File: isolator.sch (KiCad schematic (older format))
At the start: 21 parts, among them U101 NE5532

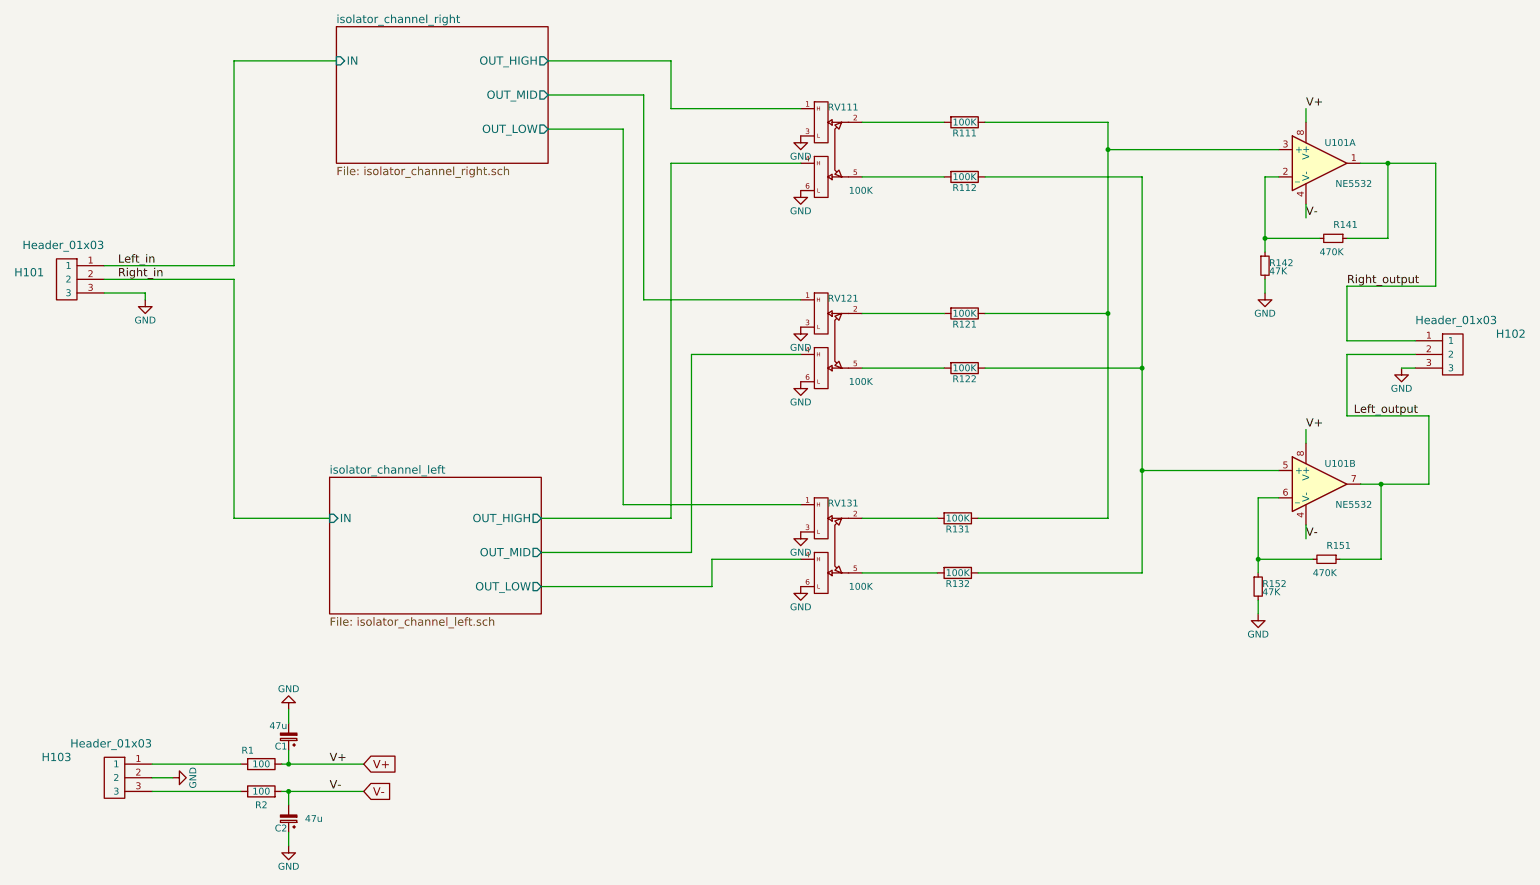
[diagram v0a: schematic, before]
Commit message: Adding active components references
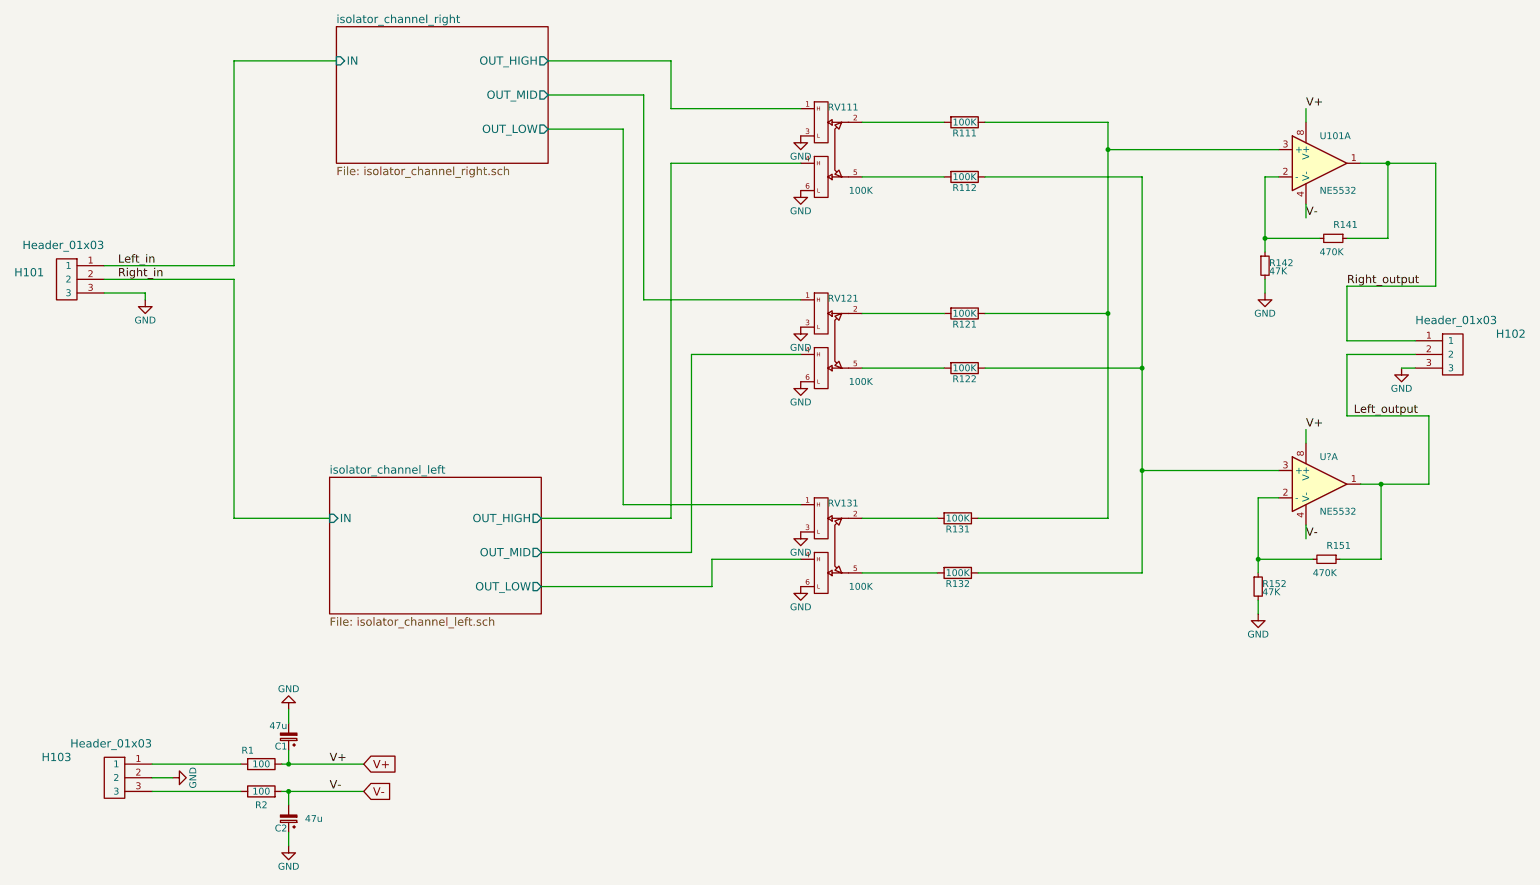
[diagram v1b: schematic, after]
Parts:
- removed U101: NE5532, Housings_DIP:DIP-8_W7.62mm_LongPads, symbol NE5532-RESCUE-isolator
- added U101, U?: NE5532, Housings_DIP:DIP-8_W7.62mm_LongPads, symbol NE5532
- R111, R112, R121, R122, R131, R132: Description (none) -> Résistances à couche métallique - Trou traversant 1/3watts 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; Distributor (none) -> Mouser; Distributor Part # (none) -> 71-CCF50-100K; Manufacturer (none) -> Vishay / Dale; Mfg_Part_# (none) -> CCF50100KFKR36; Package (none) -> 2-THT
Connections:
- net Left_output: now also U?.1
- net Right_output: now also U101.1
- net V+: now also U101.8 (V+), U?.8 (V+)
- net V-: now also U101.4 (V-), U?.4 (V-)
- net at R111.1, R121.1, R131.1: now also U101.3 (+)
- net at R112.1, R122.1, R132.1: now also U?.3 (+)
- net at R141.2, R142.1: now also U101.2 (-)
- net at R151.2, R152.1: now also U?.2 (-)

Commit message: Updating components footprints
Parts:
- gave numbers to parts that had none: 1
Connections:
- net Left_output: now also U101.7; no longer U101.1
- net at R151.2, R152.1: now also U101.6 (-); no longer U101.2 (-)
- net at R112.1, R122.1, R132.1: now also U101.5 (+); no longer U101.3 (+)
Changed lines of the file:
@@
 $EndComp
 $Comp
-L NE5532 U?
-U 1 1 5A0D725C
+L NE5532 U101
+U 2 1 5A0D725C
 P 10100 4700
-F 0 "U?" H 10100 4900 50  0000 L CNN
+F 0 "U101" H 10100 4900 50  0000 L CNN
 F 1 "NE5532" H 10100 4500 50  0000 L CNN
 F 2 "Housings_DIP:DIP-8_W7.62mm_LongPads" H 10100 4700 50  0001 C CNN
@@
 F 8 "Amplificateurs opérationnels - Amplis-Op Dual Low Noise" H 10100 4700 60  0001 C CNN "Description"
 F 9 "Texas Instruments" H 10100 4700 60  0001 C CNN "Manufacturer"
-	1    10100 4700
+	2    10100 4700
 	1    0    0    -1
 $EndComp

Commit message: Updating components references and properties
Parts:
- R111, R112, R121, R122, R131, R132, R141, R142, R151, R152: footprint Resistors_ThroughHole:Resistor_Horizontal_RM7mm -> Resistors_THT:R_Axial_DIN0204_L3.6mm_D1.6mm_P5.08mm_Horizontal
- RV111, RV121, RV131: footprint ALPS_pot:Potentiometer_ALPS_RK27112A0A16 -> potentiometers:Potentiometer_ALPS_RK27; Description (none) -> Potentiomètres Flat 20mm 100k; Distributor (none) -> Mouser; Distributor Part # (none) -> 688-RK27112A0A16; Manufacturer (none) -> ALPS; Mfg_Part_# (none) -> RK27112A0A16; Package (none) -> RK27
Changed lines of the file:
@@
 F 0 "RV111" H 6610 2560 50  0000 C CNN
 F 1 "100K" H 6740 1950 50  0000 C CNN
-F 2 "ALPS_pot:Potentiometer_ALPS_RK27112A0A16" H 6450 2250 50  0001 C CNN
-F 3 "" H 6450 2250 50  0000 C CNN
-F 4 "RK27112A0A16" H 6450 2250 60  0001 C CNN "Mfg_Part_No"
+F 2 "potentiometers:Potentiometer_ALPS_RK27" H 6450 2250 50  0001 C CNN
+F 3 "http://www.alps.com/products/WebObjects/catalog.woa/E/HTML/Potentiometer/RotaryPotentiometers/RK271/RK27112A0A16.html" H 6450 2250 50  0001 C CNN
+F 4 "RK27112A0A16" H 6450 2250 60  0001 C CNN "Mfg_Part_#"
+F 5 "Mouser" H 6450 2250 60  0001 C CNN "Distributor"
+F 6 "688-RK27112A0A16" H 6450 2250 60  0001 C CNN "Distributor Part #"
+F 7 "RK27" H 6450 2250 60  0001 C CNN "Package"
+F 8 "Potentiomètres Flat 20mm 100k" H 6450 2250 60  0001 C CNN "Description"
+F 9 "ALPS" H 6450 2250 60  0001 C CNN "Manufacturer"
+F 10 "RK27112A0A16" H 6450 2250 60  0001 C CNN "Mfg_Part_No"
 	1    6450 2250
-	1    0    0    -1
-$EndComp
-$Comp
-L DUAL_POT RV121
-U 1 1 56D771AD
-P 6450 3650
-F 0 "RV121" H 6610 3960 50  0000 C CNN
-F 1 "100K" H 6740 3350 50  0000 C CNN
-F 2 "ALPS_pot:Potentiometer_ALPS_RK27112A0A16" H 6450 3650 50  0001 C CNN
-F 3 "" H 6450 3650 50  0000 C CNN
-F 4 "RK27112A0A16" H 6450 3650 60  0001 C CNN "Mfg_Part_No"
-	1    6450 3650
-	1    0    0    -1
-$EndComp
-$Comp
-L DUAL_POT RV131
-U 1 1 56D7724C
-P 6450 5150
-F 0 "RV131" H 6610 5460 50  0000 C CNN
-F 1 "100K" H 6740 4850 50  0000 C CNN
-F 2 "ALPS_pot:Potentiometer_ALPS_RK27112A0A16" H 6450 5150 50  0001 C CNN
-F 3 "" H 6450 5150 50  0000 C CNN
-F 4 "RK27112A0A16" H 6450 5150 60  0001 C CNN "Mfg_Part_No"
-	1    6450 5150
 	1    0    0    -1
 $EndComp
@@
 F 0 "R121" V 7580 3450 50  0000 C CNN
 F 1 "100K" V 7500 3450 50  0000 C CNN
-F 2 "Resistors_ThroughHole:Resistor_Horizontal_RM7mm" V 7430 3450 50  0001 C CNN
+F 2 "Resistors_THT:R_Axial_DIN0204_L3.6mm_D1.6mm_P5.08mm_Horizontal" V 7430 3450 50  0001 C CNN
 F 3 "http://www.mouser.com/ds/2/427/ccf50-239758.pdf" H 7500 3450 50  0001 C CNN
 F 4 "CCF50100KFKR36" H 7500 3450 60  0001 C CNN "Mfg_Part_#"
@@
 	7650 2450 8800 2450
 Wire Wire Line
-	8800 2450 8800 3850
-Wire Wire Line
-	8800 3850 8800 4600
-Wire Wire Line
-	8800 4600 8800 5350
+	8800 2450 8800 5350
 Wire Wire Line
 	8800 3850 7650 3850
@@
 	8550 4950 7600 4950
 Wire Wire Line
-	8550 2050 8550 2250
-Wire Wire Line
-	8550 2250 8550 3450
-Wire Wire Line
-	8550 3450 8550 4950
+	8550 2050 8550 4950
 Wire Wire Line
 	8550 3450 7650 3450
@@
 F 0 "R142" H 9730 3120 50  0000 L CNN
 F 1 "47K" H 9730 3060 50  0000 L CNN
-F 2 "Resistors_ThroughHole:Resistor_Horizontal_RM7mm" H 9700 3100 50  0001 C CNN
+F 2 "Resistors_THT:R_Axial_DIN0204_L3.6mm_D1.6mm_P5.08mm_Horizontal" H 9700 3100 50  0001 C CNN
 F 3 "" H 9700 3100 50  0000 C CNN
 F 4 "CCF0747K0JKE36" H 9700 3100 60  0001 C CNN "Mfg_Part_No"
@@
 F 0 "R141" V 10100 2900 50  0000 L CNN
 F 1 "470K" V 10300 2800 50  0000 L CNN
-F 2 "Resistors_ThroughHole:Resistor_Horizontal_RM7mm" H 10200 2900 50  0001 C CNN
+F 2 "Resistors_THT:R_Axial_DIN0204_L3.6mm_D1.6mm_P5.08mm_Horizontal" H 10200 2900 50  0001 C CNN
 F 3 "" H 10200 2900 50  0000 C CNN
 F 4 "CCF07470KGKE36" H 10200 2900 60  0001 C CNN "Mfg_Part_No"
@@
 	9800 2450 9700 2450
 Wire Wire Line
-	9700 2450 9700 2900
-Wire Wire Line
-	9700 2900 9700 3000
+	9700 2450 9700 3000
 Wire Wire Line
 	10100 2900 9700 2900
 Connection ~ 9700 2900
 Wire Wire Line
-	10400 2350 10600 2350
-Wire Wire Line
-	10600 2350 10950 2350
+	10400 2350 10950 2350
 Wire Wire Line
 	10600 2350 10600 2900
@@
 F 0 "R152" H 9680 5470 50  0000 L CNN
 F 1 "47K" H 9680 5410 50  0000 L CNN
-F 2 "Resistors_ThroughHole:Resistor_Horizontal_RM7mm" H 9650 5450 50  0001 C CNN
+F 2 "Resistors_THT:R_Axial_DIN0204_L3.6mm_D1.6mm_P5.08mm_Horizontal" H 9650 5450 50  0001 C CNN
 F 3 "" H 9650 5450 50  0000 C CNN
 F 4 "CCF0747K0JKE36" H 9650 5450 60  0001 C CNN "Mfg_Part_No"
@@
 F 0 "R151" V 10050 5250 50  0000 L CNN
 F 1 "470K" V 10250 5150 50  0000 L CNN
-F 2 "Resistors_ThroughHole:Resistor_Horizontal_RM7mm" H 10150 5250 50  0001 C CNN
+F 2 "Resistors_THT:R_Axial_DIN0204_L3.6mm_D1.6mm_P5.08mm_Horizontal" H 10150 5250 50  0001 C CNN
 F 3 "" H 10150 5250 50  0000 C CNN
 F 4 "CCF07470KGKE36" H 10150 5250 60  0001 C CNN "Mfg_Part_No"
@@
 $EndComp
 Wire Wire Line
-	9650 4800 9650 5250
-Wire Wire Line
-	9650 5250 9650 5350
+	9650 4800 9650 5350
 Wire Wire Line
 	10050 5250 9650 5250
@@
 	9800 4800 9650 4800
 Wire Wire Line
-	10400 4700 10550 4700
-Wire Wire Line
-	10550 4700 10900 4700
+	10400 4700 10900 4700
 $Comp
 L Header_01x03 H102
@@
 $EndComp
 Wire Wire Line
-	2500 6750 2550 6750
-Wire Wire Line
-	2550 6750 3100 6750
+	2500 6750 3100 6750
 Wire Wire Line
 	2550 6750 2550 6650
 Connection ~ 2550 6750
 Wire Wire Line
-	2500 6950 2550 6950
-Wire Wire Line
-	2550 6950 3100 6950
+	2500 6950 3100 6950
 Wire Wire Line
 	2550 7050 2550 6950
@@
 F 0 "R122" V 7580 3850 50  0000 C CNN
 F 1 "100K" V 7500 3850 50  0000 C CNN
-F 2 "Resistors_ThroughHole:Resistor_Horizontal_RM7mm" V 7430 3850 50  0001 C CNN
+F 2 "Resistors_THT:R_Axial_DIN0204_L3.6mm_D1.6mm_P5.08mm_Horizontal" V 7430 3850 50  0001 C CNN
 F 3 "http://www.mouser.com/ds/2/427/ccf50-239758.pdf" H 7500 3850 50  0001 C CNN
 F 4 "CCF50100KFKR36" H 7500 3850 60  0001 C CNN "Mfg_Part_#"
@@
 F 0 "R111" V 7580 2050 50  0000 C CNN
 F 1 "100K" V 7500 2050 50  0000 C CNN
-F 2 "Resistors_ThroughHole:Resistor_Horizontal_RM7mm" V 7430 2050 50  0001 C CNN
+F 2 "Resistors_THT:R_Axial_DIN0204_L3.6mm_D1.6mm_P5.08mm_Horizontal" V 7430 2050 50  0001 C CNN
 F 3 "http://www.mouser.com/ds/2/427/ccf50-239758.pdf" H 7500 2050 50  0001 C CNN
 F 4 "CCF50100KFKR36" H 7500 2050 60  0001 C CNN "Mfg_Part_#"
@@
 F 0 "R112" V 7580 2450 50  0000 C CNN
 F 1 "100K" V 7500 2450 50  0000 C CNN
-F 2 "Resistors_ThroughHole:Resistor_Horizontal_RM7mm" V 7430 2450 50  0001 C CNN
+F 2 "Resistors_THT:R_Axial_DIN0204_L3.6mm_D1.6mm_P5.08mm_Horizontal" V 7430 2450 50  0001 C CNN
 F 3 "http://www.mouser.com/ds/2/427/ccf50-239758.pdf" H 7500 2450 50  0001 C CNN
 F 4 "CCF50100KFKR36" H 7500 2450 60  0001 C CNN "Mfg_Part_#"
@@
 F 0 "R131" V 7530 4950 50  0000 C CNN
 F 1 "100K" V 7450 4950 50  0000 C CNN
-F 2 "Resistors_ThroughHole:Resistor_Horizontal_RM7mm" V 7380 4950 50  0001 C CNN
+F 2 "Resistors_THT:R_Axial_DIN0204_L3.6mm_D1.6mm_P5.08mm_Horizontal" V 7380 4950 50  0001 C CNN
 F 3 "http://www.mouser.com/ds/2/427/ccf50-239758.pdf" H 7450 4950 50  0001 C CNN
 F 4 "CCF50100KFKR36" H 7450 4950 60  0001 C CNN "Mfg_Part_#"
@@
 F 0 "R132" V 7530 5350 50  0000 C CNN
 F 1 "100K" V 7450 5350 50  0000 C CNN
-F 2 "Resistors_ThroughHole:Resistor_Horizontal_RM7mm" V 7380 5350 50  0001 C CNN
+F 2 "Resistors_THT:R_Axial_DIN0204_L3.6mm_D1.6mm_P5.08mm_Horizontal" V 7380 5350 50  0001 C CNN
 F 3 "http://www.mouser.com/ds/2/427/ccf50-239758.pdf" H 7450 5350 50  0001 C CNN
 F 4 "CCF50100KFKR36" H 7450 5350 60  0001 C CNN "Mfg_Part_#"
@@
 	0    1    1    0
 $EndComp
+$Comp
+L DUAL_POT RV121
+U 1 1 5A0D74C1
+P 6450 3650
+F 0 "RV121" H 6610 3960 50  0000 C CNN
+F 1 "100K" H 6740 3350 50  0000 C CNN
+F 2 "potentiometers:Potentiometer_ALPS_RK27" H 6450 3650 50  0001 C CNN
+F 3 "http://www.alps.com/products/WebObjects/catalog.woa/E/HTML/Potentiometer/RotaryPotentiometers/RK271/RK27112A0A16.html" H 6450 3650 50  0001 C CNN
+F 4 "RK27112A0A16" H 6450 3650 60  0001 C CNN "Mfg_Part_#"
+F 5 "Mouser" H 6450 3650 60  0001 C CNN "Distributor"
+F 6 "688-RK27112A0A16" H 6450 3650 60  0001 C CNN "Distributor Part #"
+F 7 "RK27" H 6450 3650 60  0001 C CNN "Package"
+F 8 "Potentiomètres Flat 20mm 100k" H 6450 3650 60  0001 C CNN "Description"
+F 9 "ALPS" H 6450 3650 60  0001 C CNN "Manufacturer"
+F 10 "RK27112A0A16" H 6450 3650 60  0001 C CNN "Mfg_Part_No"
+	1    6450 3650
+	1    0    0    -1
+$EndComp
+$Comp
+L DUAL_POT RV131
+U 1 1 5A0D77F6
+P 6450 5150
+F 0 "RV131" H 6610 5460 50  0000 C CNN
+F 1 "100K" H 6740 4850 50  0000 C CNN
+F 2 "potentiometers:Potentiometer_ALPS_RK27" H 6450 5150 50  0001 C CNN
+F 3 "http://www.alps.com/products/WebObjects/catalog.woa/E/HTML/Potentiometer/RotaryPotentiometers/RK271/RK27112A0A16.html" H 6450 5150 50  0001 C CNN
+F 4 "RK27112A0A16" H 6450 5150 60  0001 C CNN "Mfg_Part_#"
+F 5 "Mouser" H 6450 5150 60  0001 C CNN "Distributor"
+F 6 "688-RK27112A0A16" H 6450 5150 60  0001 C CNN "Distributor Part #"
+F 7 "RK27" H 6450 5150 60  0001 C CNN "Package"
+F 8 "Potentiomètres Flat 20mm 100k" H 6450 5150 60  0001 C CNN "Description"
+F 9 "ALPS" H 6450 5150 60  0001 C CNN "Manufacturer"
+F 10 "RK27112A0A16" H 6450 5150 60  0001 C CNN "Mfg_Part_No"
+	1    6450 5150
+	1    0    0    -1
+$EndComp
 $EndSCHEMATC
